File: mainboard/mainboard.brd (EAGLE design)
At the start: 158.8 x 159.4 mm, 106 parts, among them T1 NPN_BC817,215, T2 NPN_BC817,215, T3 NPN_BC817,215, U1 CD4051BM, X1 JST-XH-10-PIN-LONG-PAD, X2 JST-XH-10-PIN-LONG-PAD, X3 JST-XH-10-PIN-LONG-PAD, X4 JST-XH-10-PIN-LONG-PAD, X5 JST-XH-10-PIN-LONG-PAD

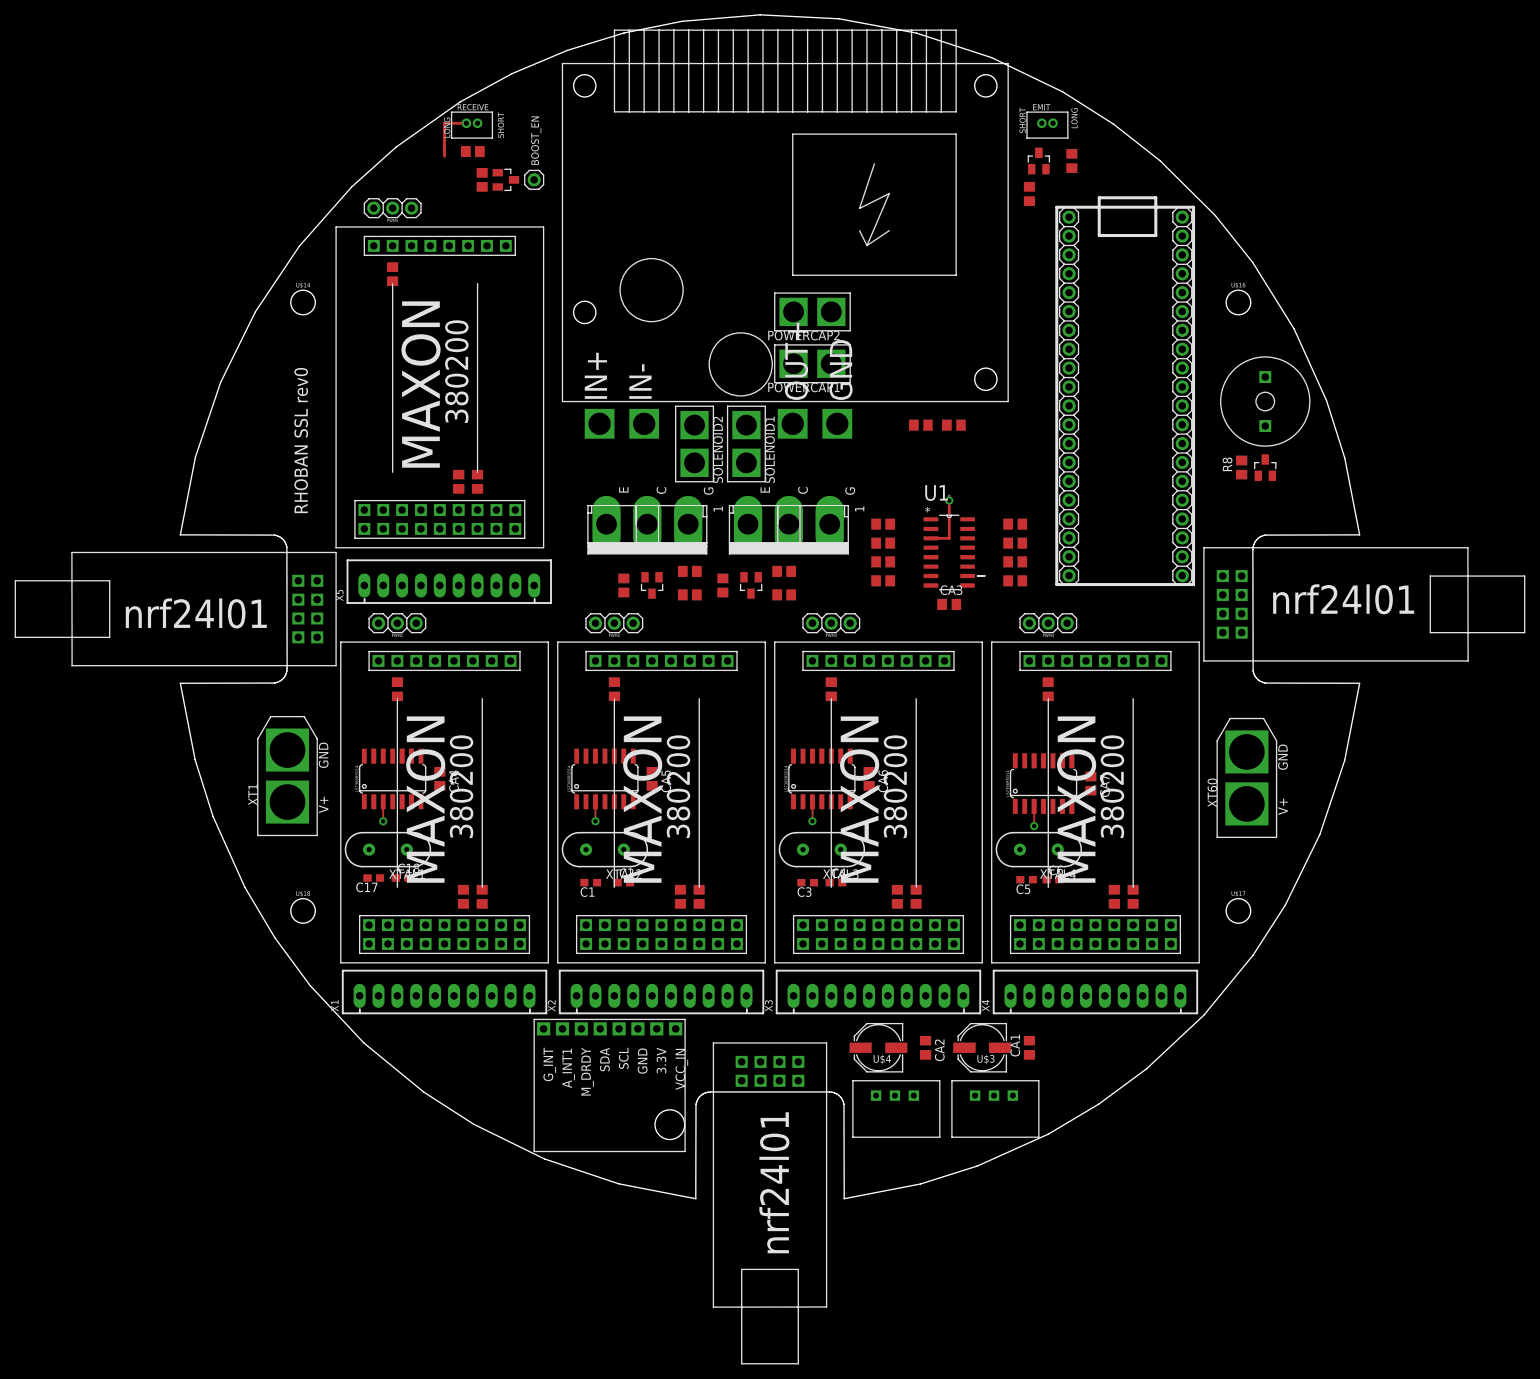
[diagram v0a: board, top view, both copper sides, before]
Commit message: Updating mainboard, using brushless drivers [wip]
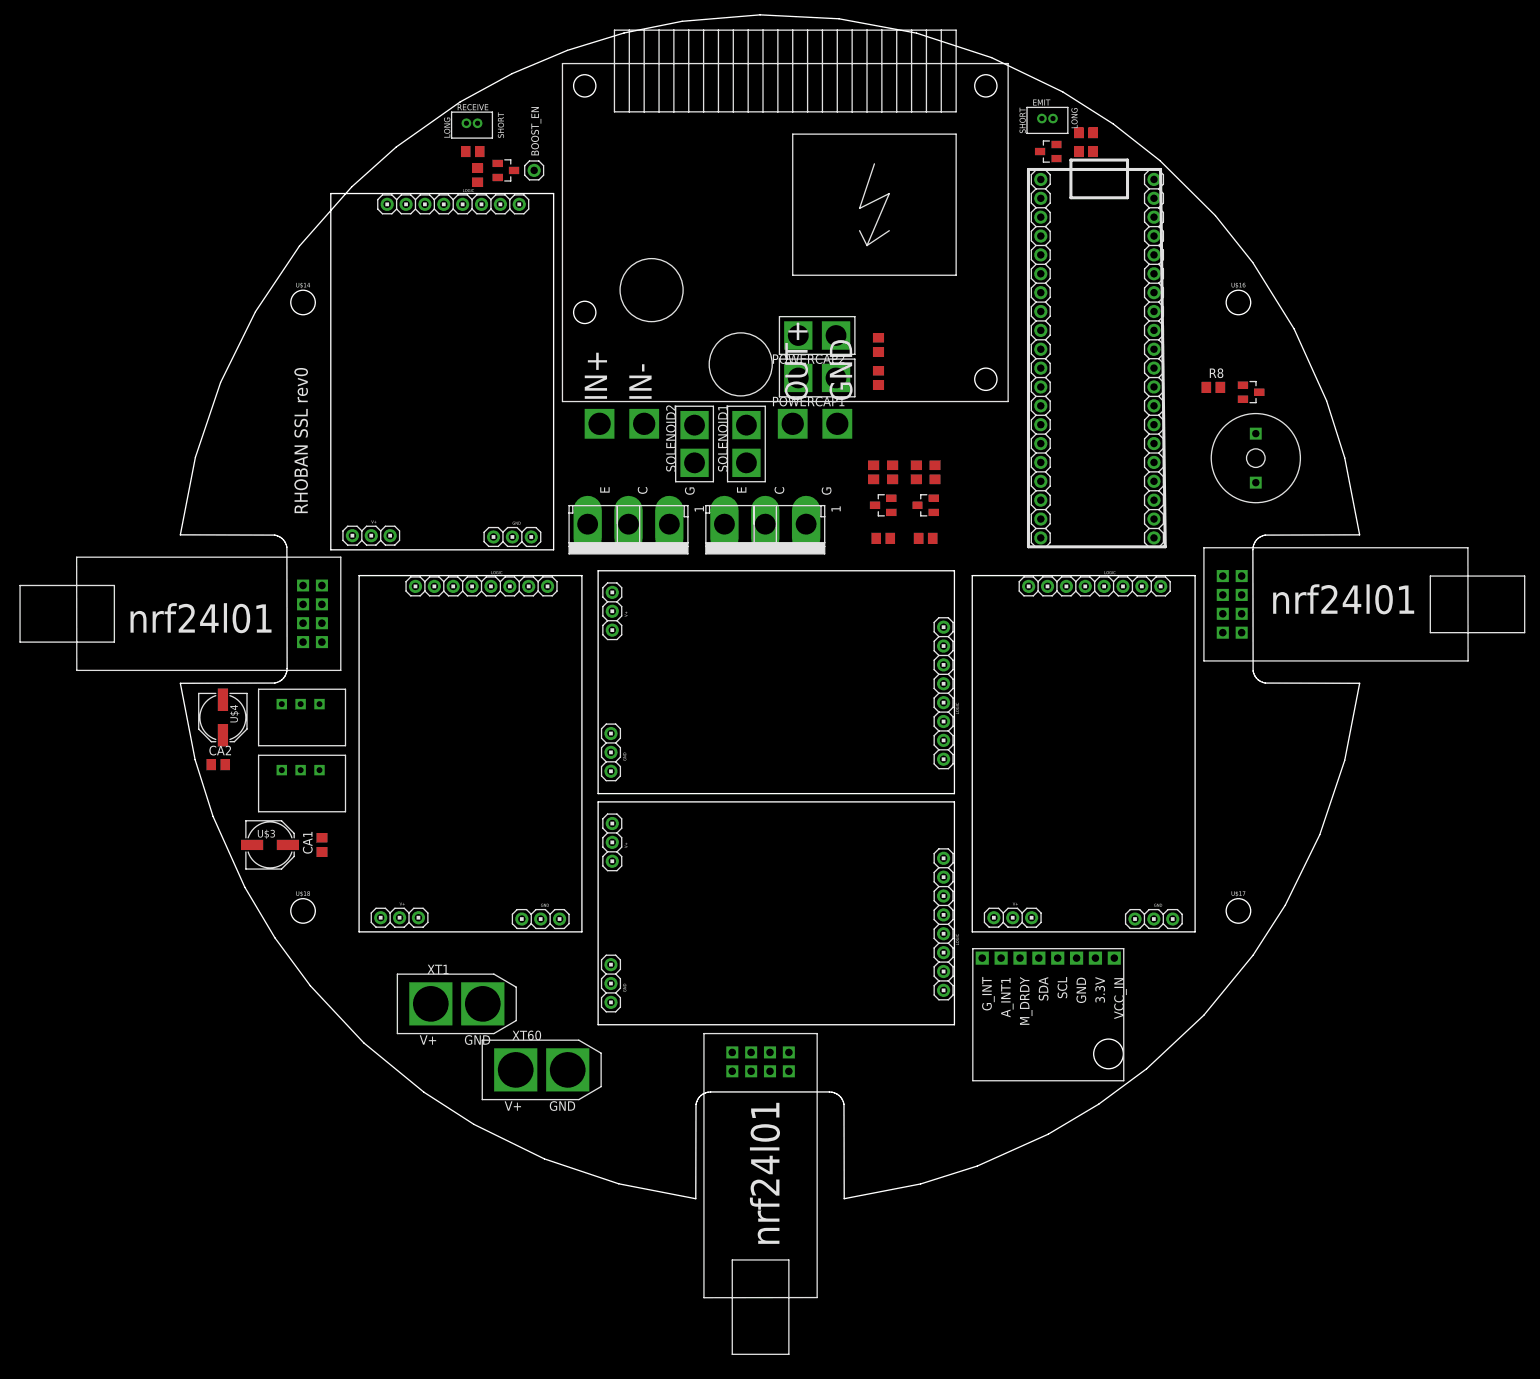
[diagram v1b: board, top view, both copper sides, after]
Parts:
- removed C1, C17, C18, C2, C3, C4, C5, C6: 15pF, rhoban:C0603
- removed CA3, CA4, CA5, CA6, CA7: C_EU-100NF, rhoban:C0805
- removed ENC1, ENC2, ENC3, ENC4: LS7366RSO14, rhoban:SO14
- removed PWM1, PWM2, PWM3, PWM4, PWM5: CONNEC_1X03, rhoban:CONNEC_1X03
- removed R10, R11, R12, R13, R14, R15, R7, R9: 3K, rhoban:R0805
- removed R16, R17, R19, R20, R22, R23, R25, R26, R28, R29: 1K, rhoban:R0805
- removed R18, R21, R24, R27, R30: 24k, rhoban:R0805
- removed U$10, U$6, U$7, U$8, U$9: MAXON380200, rhoban:MAXON380200
- removed U1: CD4051BM, rhoban:SOIC127P600X175-16N
- removed X1, X2, X3, X4, X5: JST-XH-10-PIN-LONG-PAD, Rembrandt Electronics - JST XH Connectors v1-0:JST-XH-10-PACKAGE-LONG-PAD
- removed XTAL1, XTAL2, XTAL3, XTAL4: 40Mhz, rhoban:HC49US
- added DRIVER1, DRIVER2, DRIVER3, DRIVER4, DRIVER5: RHOBAN_BL_DRIVER, rhoban:RHOBAN_BL_DRIVER
- moved XT60 112.6 mm to (-35.6, -63.5), turned to 0 degrees
- moved REG3.3V 103.1 mm to (-54.0, -17.1)
- moved CA2 102.6 mm to (-71.1, -18.4), turned to 0 degrees
- moved U$3 99.7 mm to (-64.1, -29.2), turned to 0 degrees
- moved CA1 99.1 mm to (-57.1, -29.2)
- moved U$4 98.8 mm to (-70.5, -12.1), turned to 270 degrees
- moved REG5V 95.8 mm to (-54.0, -8.26)
- moved U$2 59.8 mm to (31.8, -44.5)
- moved R3 35.5 mm to (18.4, 12.1), turned to 0 degrees
- moved T1 32.9 mm to (18.4, 16.5), turned to 90 degrees
- moved R1 30.4 mm to (19.7, 21.0), turned to 270 degrees
- moved R2 29.8 mm to (17.1, 21.0), turned to 270 degrees
- moved XT1 28.8 mm to (-47.0, -54.6), turned to 0 degrees
- moved R33 28.0 mm to (24.1, 12.1), turned to 0 degrees
- moved T3 25.9 mm to (24.1, 16.5), turned to 90 degrees
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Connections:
- removed net CS1: ENC1.4, R7.2, U1.13
- removed net CS2: ENC2.4, R9.2, U1.14
- removed net CS3: ENC3.4, R10.2, U1.15
- removed net CS4: ENC4.4, R11.2, U1.12
- removed net CS5: COM1.CSN, R12.2, U1.1
- removed net CS6: COM2.CSN, R13.2, U1.5
- removed net CS7: COM3.CSN, R14.2, U1.2
- removed net CS8: R15.2, U1.4
- removed net CSA1: MAPLE.X20, U1.11
- removed net CSA2: MAPLE.X21, U1.10
- removed net CSA3: MAPLE.X22, U1.9
- removed net INDEX: ENC1.10, ENC2.10, ENC3.10, ENC4.10, MAPLE.X26
- removed net M1_A: ENC1.12, X1.9
- removed net M1_B: ENC1.11, X1.10
- removed net M1_DIR: MAPLE.X13, U$6.23
- removed net M1_HALL1: U$6.13, X1.6
- removed net M1_HALL2: U$6.15, X1.7
- removed net M1_HALL3: U$6.17, X1.8
- removed net M1_SPEED: MAPLE.X3, PWM1.3, U$6.26
- removed net M1_W1: U$6.1, U$6.2, X1.1
- removed net M1_W2: U$6.3, U$6.4, X1.2
- removed net M1_W3: U$6.5, U$6.6, X1.3
- removed net M2_A: ENC2.12, X2.9
- removed net M2_B: ENC2.11, X2.10
- removed net M2_DIR: MAPLE.X14, U$7.23
- removed net M2_HALL1: U$7.13, X2.6
- removed net M2_HALL2: U$7.15, X2.7
- removed net M2_HALL3: U$7.17, X2.8
- removed net M2_SPEED: MAPLE.X4, PWM2.3, U$7.26
- removed net M2_W1: U$7.1, U$7.2, X2.1
- removed net M2_W2: U$7.3, U$7.4, X2.2
- removed net M2_W3: U$7.5, U$7.6, X2.3
- removed net M3_A: ENC3.12, X3.9
- removed net M3_B: ENC3.11, X3.10
- removed net M3_DIR: MAPLE.X17, U$8.23
- removed net M3_HALL1: U$8.13, X3.6
- removed net M3_HALL2: U$8.15, X3.7
- removed net M3_HALL3: U$8.17, X3.8
- removed net M3_SPEED: MAPLE.X5, PWM3.3, U$8.26
- removed net M3_W1: U$8.1, U$8.2, X3.1
- removed net M3_W2: U$8.3, U$8.4, X3.2
- removed net M3_W3: U$8.5, U$8.6, X3.3
- removed net M4_A: ENC4.12, X4.9
- removed net M4_B: ENC4.11, X4.10
- removed net M4_DIR: MAPLE.X18, U$9.23
- removed net M4_HALL1: U$9.13, X4.6
- removed net M4_HALL2: U$9.15, X4.7
- removed net M4_HALL3: U$9.17, X4.8
- removed net M4_SPEED: MAPLE.X8, PWM4.3, U$9.26
- removed net M4_W1: U$9.1, U$9.2, X4.1
- removed net M4_W2: U$9.3, U$9.4, X4.2
- removed net M4_W3: U$9.5, U$9.6, X4.3
- removed net M5_DIR: MAPLE.X19, U$10.23
- removed net M5_HALL1: U$10.13, X5.6
- removed net M5_HALL2: U$10.15, X5.7
- removed net M5_HALL3: U$10.17
- removed net M5_SPEED: MAPLE.X9, PWM5.3, U$10.26
- removed net M5_W1: U$10.1, U$10.2, X5.1
- removed net M5_W2: U$10.3, U$10.4, X5.2
- removed net M5_W3: U$10.5, U$10.6, X5.3
- removed net MOTORS_EN: U$10.22, U$6.22, U$7.22, U$8.22, U$9.22
- removed net MT_HALL3: X5.8
- removed net N$10: R16.2, U$6.20
- removed net N$12: R17.2, U$6.21
- removed net N$13: C1.2, ENC2.1, XTAL2.2
- removed net N$14: C2.2, ENC2.2, XTAL2.1
- removed net N$15: R19.2, U$7.20
- removed net N$16: R18.2, U$6.25
- removed net N$18: R20.2, U$7.21
- removed net N$19: C17.2, ENC1.1, XTAL1.2
- removed net N$20: C18.2, ENC1.2, XTAL1.1
- removed net N$21: R21.2, U$7.25
- removed net N$22: C3.2, ENC3.1, XTAL3.2
- removed net N$23: C4.2, ENC3.2, XTAL3.1
- removed net N$24: R22.2, U$8.20
- removed net N$25: R23.2, U$8.21
- removed net N$26: R24.2, U$8.25
- removed net N$27: C5.2, ENC4.1, XTAL4.2
- removed net N$28: C6.2, ENC4.2, XTAL4.1
- removed net N$29: R25.2, U$9.20
- removed net N$30: R26.2, U$9.21
- removed net N$31: R27.2, U$9.25
- removed net N$32: R28.2, U$10.20
- removed net N$33: R29.2, U$10.21
- removed net N$34: R30.2, U$10.25
- removed net N$8: REG5V.P$2
- removed net N$9: REG3.3V.P$2
- new net CS_COM_1: COM1.CSN, MAPLE.X20
- new net CS_COM_2: COM2.CSN, MAPLE.X21
- new net CS_COM_3: COM3.CSN, MAPLE.X22
- new net DRIVERS_CS1: DRIVER1.CS, MAPLE.X7
- new net DRIVERS_CS2: DRIVER2.CS, MAPLE.X26
- new net DRIVERS_CS3: DRIVER3.CS, MAPLE.X19
- new net DRIVERS_CS4: DRIVER4.CS, MAPLE.X18
- new net DRIVERS_CS5: DRIVER5.CS, MAPLE.X17
- new net DRIVERS_MISO: DRIVER1.MISO, DRIVER2.MISO, DRIVER3.MISO, DRIVER4.MISO, DRIVER5.MISO, MAPLE.X5
- new net DRIVERS_MOSI: DRIVER1.MOSI, DRIVER2.MOSI, DRIVER3.MOSI, DRIVER4.MOSI, DRIVER5.MOSI, MAPLE.X4
- new net DRIVERS_SCK: DRIVER1.SCK, DRIVER2.SCK, DRIVER3.SCK, DRIVER4.SCK, DRIVER5.SCK, MAPLE.X6
- new net VMID: DRIVER1.VDRIVER, DRIVER2.VDRIVER, DRIVER3.VDRIVER, DRIVER4.VDRIVER, DRIVER5.VDRIVER, XT1.GND, XT60.V+
- net 3.3: now also DRIVER1.3.3, DRIVER2.3.3, DRIVER3.3.3, DRIVER4.3.3, DRIVER5.3.3; no longer CA3.1, R10.1, R11.1, R12.1, R13.1, R14.1, R15.1, R7.1, R9.1, U1.16
- net CAP: now also MAPLE.X3; no longer MAPLE.X6
- net GND: now also DRIVER1.GND, DRIVER1.GND2, DRIVER1.GND3, DRIVER1.GND4, DRIVER2.GND, DRIVER2.GND2, DRIVER2.GND3, DRIVER2.GND4, DRIVER3.GND, DRIVER3.GND2, DRIVER3.GND3, DRIVER3.GND4, DRIVER4.GND, DRIVER4.GND2, DRIVER4.GND3, DRIVER4.GND4, DRIVER5.GND, DRIVER5.GND2, DRIVER5.GND3, DRIVER5.GND4, REG3.3V.P$2, REG5V.P$2; no longer C1.1, C17.1, C18.1, C2.1, C3.1, C4.1, C5.1, C6.1, CA3.2, CA4.2, CA5.2, CA6.2, CA7.2, ENC1.3, ENC2.3, ENC3.3, ENC4.3, PWM1.1, PWM2.1, PWM3.1, PWM4.1, PWM5.1, R16.1, R18.1, R19.1, R21.1, R22.1, R24.1, R25.1, R27.1, R28.1, R30.1, U$10.10, U$10.14, U$10.16, U$10.24, U$10.9, U$6.10, U$6.14, U$6.16, U$6.24, U$6.9, U$7.10, U$7.14, U$7.16, U$7.24, U$7.9, U$8.10, U$8.14, U$8.16, U$8.24, U$8.9, U$9.10, U$9.14, U$9.16, U$9.24, U$9.9, U1.3, U1.6, U1.7, U1.8, X1.4, X2.4, X3.4, X4.4, X5.4, XT1.GND
- net MISO: no longer ENC1.6, ENC2.6, ENC3.6, ENC4.6
- net MOSI: no longer ENC1.7, ENC2.7, ENC3.7, ENC4.7
- net SCK: no longer ENC1.5, ENC2.5, ENC3.5, ENC4.5
- net VCC: now also DRIVER1.VCC, DRIVER2.VCC, DRIVER3.VCC, DRIVER4.VCC, DRIVER5.VCC; no longer CA4.1, CA5.1, CA6.1, CA7.1, ENC1.14, ENC2.14, ENC3.14, ENC4.14, R17.1, R20.1, R23.1, R26.1, R29.1, U$10.11, U$6.11, U$7.11, U$8.11, U$9.11, X1.5, X2.5, X3.5, X4.5, X5.5
- net VIN: now also DRIVER1.V+1, DRIVER1.V+2, DRIVER1.V+3, DRIVER2.V+1, DRIVER2.V+2, DRIVER2.V+3, DRIVER3.V+1, DRIVER3.V+2, DRIVER3.V+3, DRIVER4.V+1, DRIVER4.V+2, DRIVER4.V+3, DRIVER5.V+1, DRIVER5.V+2, DRIVER5.V+3; no longer U$10.7, U$10.8, U$6.7, U$6.8, U$7.7, U$7.8, U$8.7, U$8.8, U$9.7, U$9.8, XT60.V+
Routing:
- net GND: track 26.1 -> 0.00 mm, vias 5 -> 0

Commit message: mainboard
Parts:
- removed CA1, CA2: C_EU-100NF, rhoban:C0805
- added C1, C7: 1uF, SparkFun-Passives:0805@1
- added D1, D2, D3, D4, D5: (no value), SparkFun-DiscreteSemi:SOD-323
- added R10, R7: 10K, rhoban:R0805
- added R11, R9: 1K, rhoban:R0805
- R5: value 110 -> 62
- moved COM2 8.26 mm to (64.1, -1.27), flipped to the bottom, turned to 90 degrees
- moved COM1 8.25 mm to (-57.1, 6.35), flipped to the bottom, turned to 270 degrees
- moved COM3 6.38 mm to (-0.64, -57.8), flipped to the bottom
- moved U$3 4.45 mm to (-59.7, -29.2)
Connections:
- new net BAT1: MAPLE.X8, R7.1, R9.2
- new net BAT2: MAPLE.X9, R10.1, R11.2
- new net N$10: D4.1, DRIVER5.VDRIVER
- new net N$12: D2.1, DRIVER3.VDRIVER
- new net N$13: D1.1, DRIVER2.VDRIVER
- new net N$8: D5.1, DRIVER1.VDRIVER
- new net N$9: D3.1, DRIVER4.VDRIVER
- net 3.3: now also C7.2; no longer CA1.1
- net GND: now also C1.1, C7.1, R11.1, R9.1; no longer CA1.2, CA2.2
- net VBOOST: now also R10.2, R7.2
- net VCC: now also C1.2; no longer CA2.1
- net VMID: now also D1.2, D2.2, D3.2, D4.2, D5.2; no longer DRIVER1.VDRIVER, DRIVER2.VDRIVER, DRIVER3.VDRIVER, DRIVER4.VDRIVER, DRIVER5.VDRIVER

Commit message: mainboard
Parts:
- moved SOLENOID1 12.9 mm to (-6.75, 33.3), turned to 270 degrees
- moved SOLENOID2 12.8 mm to (-0.52, 33.3), turned to 270 degrees
- moved U$1 3.82 mm to (-13.9, 17.2)
- moved U$11 3.34 mm to (3.29, 17.2)
- moved MAPLE 2.85 mm to (57.1, 58.6)
- moved XT1 1.95 mm to (-48.2, -53.1)
- moved XT60 1.46 mm to (-36.8, -62.8)
- moved R4 1.03 mm to (45.5, 63.1)
- moved R34 0.75 mm to (18.5, 33.7)
- moved R35 0.75 mm to (18.5, 38.1)
- moved C1 0.57 mm to (-69.8, -17.7), turned to 0 degrees
- moved U$4 0.55 mm to (-71.0, -11.9), turned to 90 degrees
- moved U$2 0.35 mm to (32.0, -44.2)
- moved POWERCAP1 0.25 mm to (11.8, 33.7)
- moved POWERCAP2 0.25 mm to (11.8, 39.4)
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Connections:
- new net COM_CE: COM1.CE, COM2.CE, COM3.CE, MAPLE.X13
- net 3.3: no longer COM1.CE, COM2.CE, COM3.CE
- net VBOOST: no longer R10.2, R7.2
- net VIN: now also R10.2
- net VMID: now also R7.2
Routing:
- net GND: track 0.00 -> 89.1 mm
- net VBOOST: track 0.00 -> 26.0 mm
- net N$2: track 0.00 -> 13.5 mm
- net N$36: track 0.00 -> 11.6 mm
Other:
- board text added: "REV0"
- board text added: "RHOBAN SSL MAINBOARD"
